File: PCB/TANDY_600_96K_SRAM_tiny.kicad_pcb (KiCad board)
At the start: 2 copper layers, 68.6 x 16.5 mm, 5 parts, among them J1 DIN41612-44-mounts, U1 628128_TSOP32, U2 74HC148

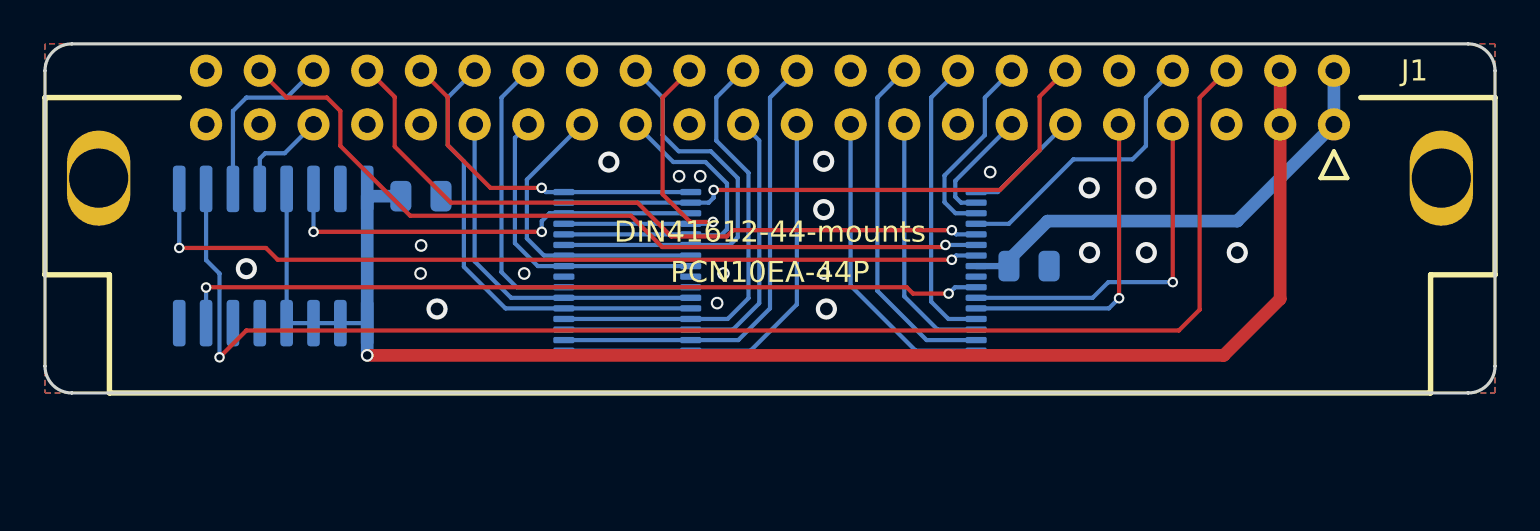
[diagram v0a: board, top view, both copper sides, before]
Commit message: silkscreen, symbols, footprints touchups
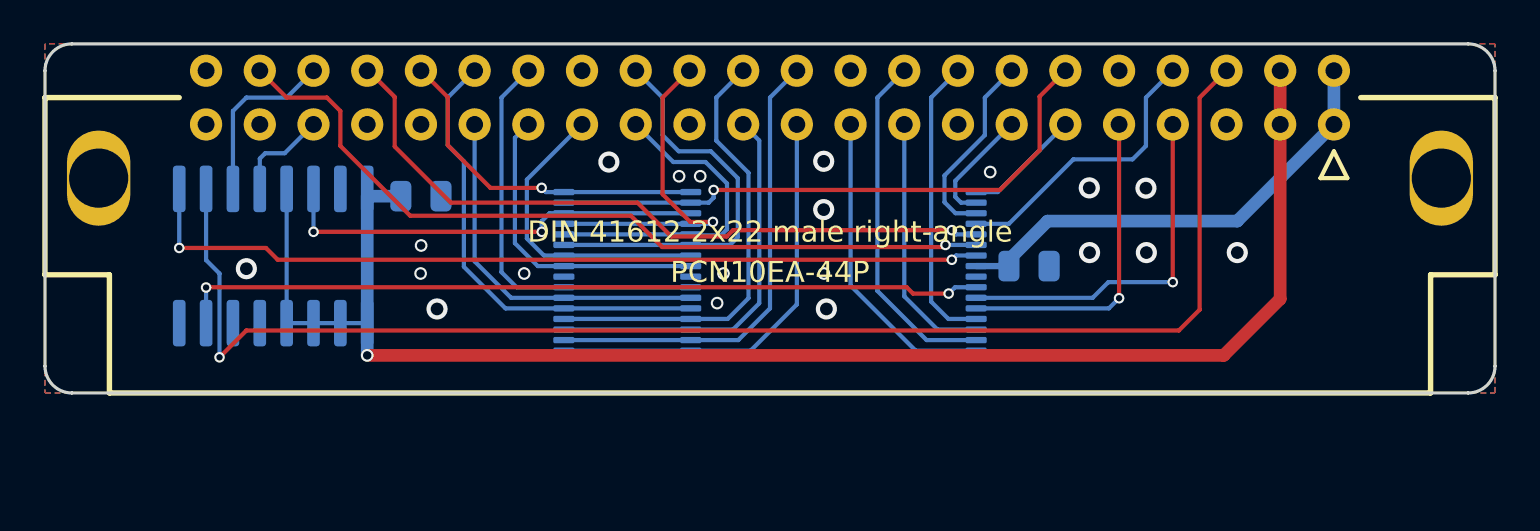
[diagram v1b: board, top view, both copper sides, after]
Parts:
- J1: value DIN41612-44-mounts -> DIN 41612 2x22 male right-angle; footprint 000_LOCAL:DIN41612-44P-male-horiz -> 000_LOCAL:DIN 41612 2x22 male right-angle
- U1: value 628128_TSOP32 -> 628128_TSOP
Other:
- board text added: "1A"
- board text added: "1B"
- board text added: "22A"
- board text added: "22B"
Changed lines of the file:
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@@
   (title_block
     (title "TANDY 600 96K SRAM tiny")
-    (date "2022-09-18")
-    (rev "001")
+    (date "2022-09-19")
+    (rev "002")
     (company "Brian K. White - b.kenyon.w@gmail.com")
     (comment 1 "LICENSE: CC-BY-SA 4.0")
@@
   (net 39 "unconnected-(U2-Pad6)")
   (net 40 "unconnected-(U2-Pad15)")
-  (footprint "000_LOCAL:DIN41612-44P-male-horiz" (layer "F.Cu")
+  (footprint "000_LOCAL:DIN 41612 2x22 male right-angle" (layer "F.Cu")
     (at 146.05 97.155)
     (property "Sheetfile" "TANDY_600_96K_SRAM_tiny.kicad_sch")
     (property "Sheetname" "")
     (attr through_hole)
-    (fp_text reference "J1" (at 30.48 -1.27) (layer "F.SilkS")
+    (fp_text reference "J1" (at 30.48 -1.27) (layer "F.SilkS") hide
       (effects (font (size 1 1) (thickness 0.15)))
     )
-    (fp_text value "DIN41612-44-mounts" (at 0 6.35) (layer "F.SilkS")
+    (fp_text value "DIN 41612 2x22 male right-angle" (at 0 6.35) (layer "F.SilkS")
       (effects (font (size 1 1) (thickness 0.15)))
     )
-    (fp_line (start 27.305 3.81) (end 26.67 2.54) (layer "F.SilkS") (width 0.2))
     (fp_line (start 34.29 8.382) (end 31.242 8.382) (layer "F.SilkS") (width 0.254))
-    (fp_line (start 31.242 13.97) (end -31.242 13.97) (layer "F.SilkS") (width 0.254))
     (fp_line (start -31.242 8.382) (end -34.29 8.382) (layer "F.SilkS") (width 0.254))
     (fp_line (start 34.29 0) (end 34.29 8.382) (layer "F.SilkS") (width 0.254))
+    (fp_line (start -31.242 13.97) (end -31.242 8.382) (layer "F.SilkS") (width 0.254))
+    (fp_line (start 31.242 13.97) (end 31.242 8.382) (layer "F.SilkS") (width 0.254))
+    (fp_line (start -34.29 0) (end -34.29 8.382) (layer "F.SilkS") (width 0.254))
+    (fp_line (start 27.305 3.81) (end 26.67 2.54) (layer "F.SilkS") (width 0.2))
+    (fp_line (start 31.242 13.97) (end -31.242 13.97) (layer "F.SilkS") (width 0.254))
+    (fp_line (start 26.67 2.54) (end 26.035 3.81) (layer "F.SilkS") (width 0.2))
     (fp_line (start -27.94 0) (end -34.29 0) (layer "F.SilkS") (width 0.254))
-    (fp_line (start -34.29 0) (end -34.29 8.382) (layer "F.SilkS") (width 0.254))
-    (fp_line (start 31.242 13.97) (end 31.242 8.382) (layer "F.SilkS") (width 0.254))
     (fp_line (start 27.94 0) (end 34.29 0) (layer "F.SilkS") (width 0.254))
-    (fp_line (start -31.242 13.97) (end -31.242 8.382) (layer "F.SilkS") (width 0.254))
     (fp_line (start 26.035 3.81) (end 27.305 3.81) (layer "F.SilkS") (width 0.2))
-    (fp_line (start 26.67 2.54) (end 26.035 3.81) (layer "F.SilkS") (width 0.2))
     (fp_line (start -28 7.57) (end 28 7.57) (layer "Dwgs.User") (width 0.15))
     (pad "1A" thru_hole circle (at 26.67 1.27) (size 1.524 1.524) (drill 0.8) (layers *.Cu *.Mask)
@@
     (pad "22B" thru_hole circle (at -26.67 -1.27) (size 1.524 1.524) (drill 0.8) (layers *.Cu *.Mask)
       (net 1 "GND") (pinfunction "22B") (pintype "passive"))
-    (pad "S" thru_hole oval (at -31.75 3.81) (size 2.999999 4.500001) (drill 2.799999) (layers *.Cu *.Mask)
-      (net 1 "GND") (pinfunction "mount_holes") (pintype "free") (zone_connect 2))
-    (pad "S" thru_hole oval (at 31.75 3.81) (size 2.999999 4.500001) (drill 2.799999) (layers *.Cu *.Mask)
-      (net 1 "GND") (pinfunction "mount_holes") (pintype "free") (zone_connect 2))
+    (pad "S1" thru_hole oval (at 31.75 3.81) (size 2.999999 4.500001) (drill 2.799999) (layers *.Cu *.Mask)
+      (net 1 "GND") (pinfunction "mount") (pintype "passive") (zone_connect 2))
+    (pad "S2" thru_hole oval (at -31.75 3.81) (size 2.999999 4.500001) (drill 2.799999) (layers *.Cu *.Mask)
+      (net 1 "GND") (pinfunction "mount") (pintype "passive") (zone_connect 2))
     (model "${KIPRJMOD}/000_LOCAL.pretty/3d/PCN10EA-44P.step"
       (offset (xyz 0 -7.30758 0))
@@
       (effects (font (size 1 1) (thickness 0.15)) (justify mirror))
     )
-    (fp_text value "628128_TSOP32" (at -3 -1.27) (layer "B.SilkS")
+    (fp_text value "628128_TSOP" (at -3 -1.27) (layer "B.SilkS")
       (effects (font (size 1 1) (thickness 0.15)) (justify mirror))
     )
@@
   (gr_line (start 179.07 111.125) (end 113.03 111.125) (layer "Edge.Cuts") (width 0.15))
   (gr_line (start 180.34 95.885) (end 180.34 109.855) (layer "Edge.Cuts") (width 0.15))
+  (gr_text "22B" (at 118.11 95.85) (layer "B.SilkS")
+    (effects (font (size 1 1) (thickness 0.15)) (justify left mirror))
+  )
+  (gr_text "22A" (at 118.11 98.39) (layer "B.SilkS")
+    (effects (font (size 1 1) (thickness 0.15)) (justify left mirror))
+  )
+  (gr_text "1A" (at 173.99 98.39) (layer "B.SilkS")
+    (effects (font (size 1 1) (thickness 0.15)) (justify right mirror))
+  )
+  (gr_text "1B" (at 173.99 95.85) (layer "B.SilkS")
+    (effects (font (size 1 1) (thickness 0.15)) (justify right mirror))
+  )
   (gr_text "${COMMENT2}  ${TITLE}  v${REVISION}" (at 146.05 110.109) (layer "B.SilkS")
     (effects (font (size 1 1) (thickness 0.15)) (justify mirror))

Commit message: add alternative tiny layout, lengthen tsop footprint slightly
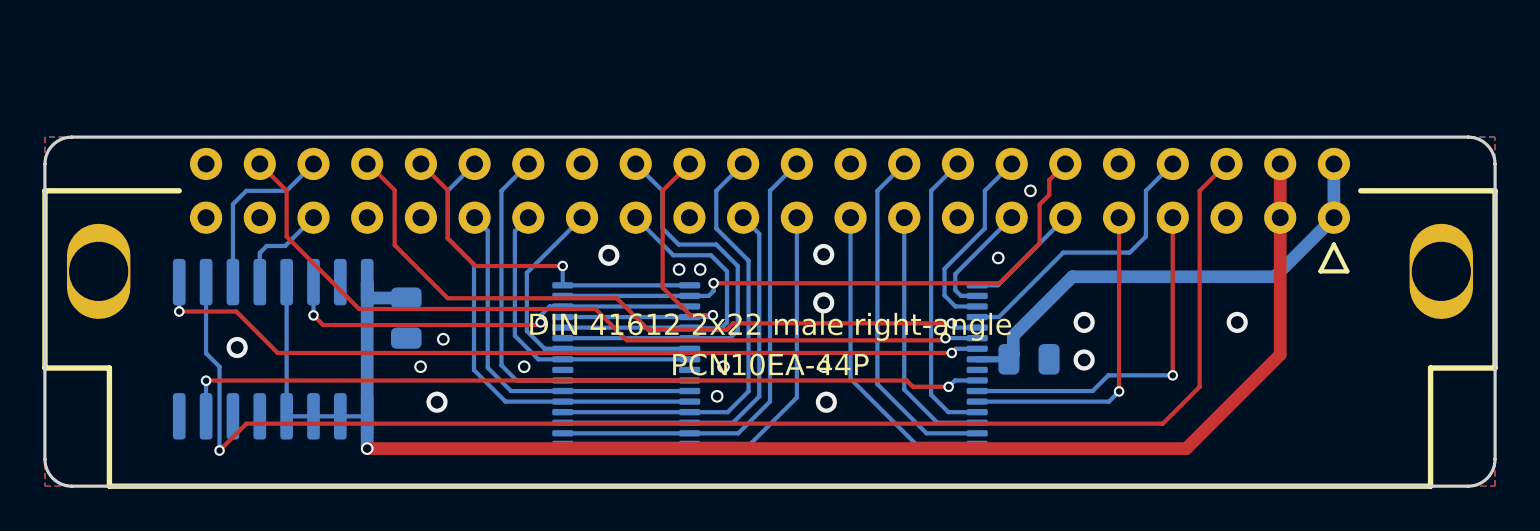
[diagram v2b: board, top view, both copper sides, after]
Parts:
- moved C2 5.81 mm to (128.8, 107.6), turned to -90 degrees
- moved C1 4.41 mm to (158.3, 109.5)
- moved J1 4.41 mm to (146.1, 101.6)
- moved U1 4.41 mm to (146.1, 109.8)
- moved U2 4.41 mm to (122.6, 109.1)
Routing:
- net /A15: track 40.3 -> 39.5 mm
- net GND: vias 20 -> 19
